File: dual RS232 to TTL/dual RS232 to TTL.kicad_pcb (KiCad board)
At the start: 2 copper layers, 51 x 15.9 mm, 11 parts, among them J1 Conn2x4, J2 Conn2x3, U1 MAX3232EEUE

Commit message: PCB acabada
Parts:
- J1: footprint Connector_Molex:Molex_Nano-Fit_105314-xx08_2x04_P2.50mm_Horizontal -> Herranz - Conn Molex:Molex_Nano-Fit_105314-xx08_2x04_P2.50mm_Horizontal
- J2: footprint Connector_Molex:Molex_Nano-Fit_105314-xx06_2x03_P2.50mm_Horizontal -> Herranz - Conn Molex:Molex_Nano-Fit_105314-xx06_2x03_P2.50mm_Horizontal
- moved C4 4.35 mm to (108.9, 78.8), turned to 90 degrees
- moved C2 4.04 mm to (107.6, 78.8), turned to 90 degrees
- moved C1 3.35 mm to (105.9, 80.3)
- moved F1 2.49 mm to (103.5, 79.3)
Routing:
- net +3V3: track 7.69 -> 5.18 mm
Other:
- board text added: "Dual RS232 to TTL"
- board text added: "https://github.com/herranz/dual-rs232-to-ttl"

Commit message: añadido de la licencia en la PCB
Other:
- board text added: "CERN-OHL-W"

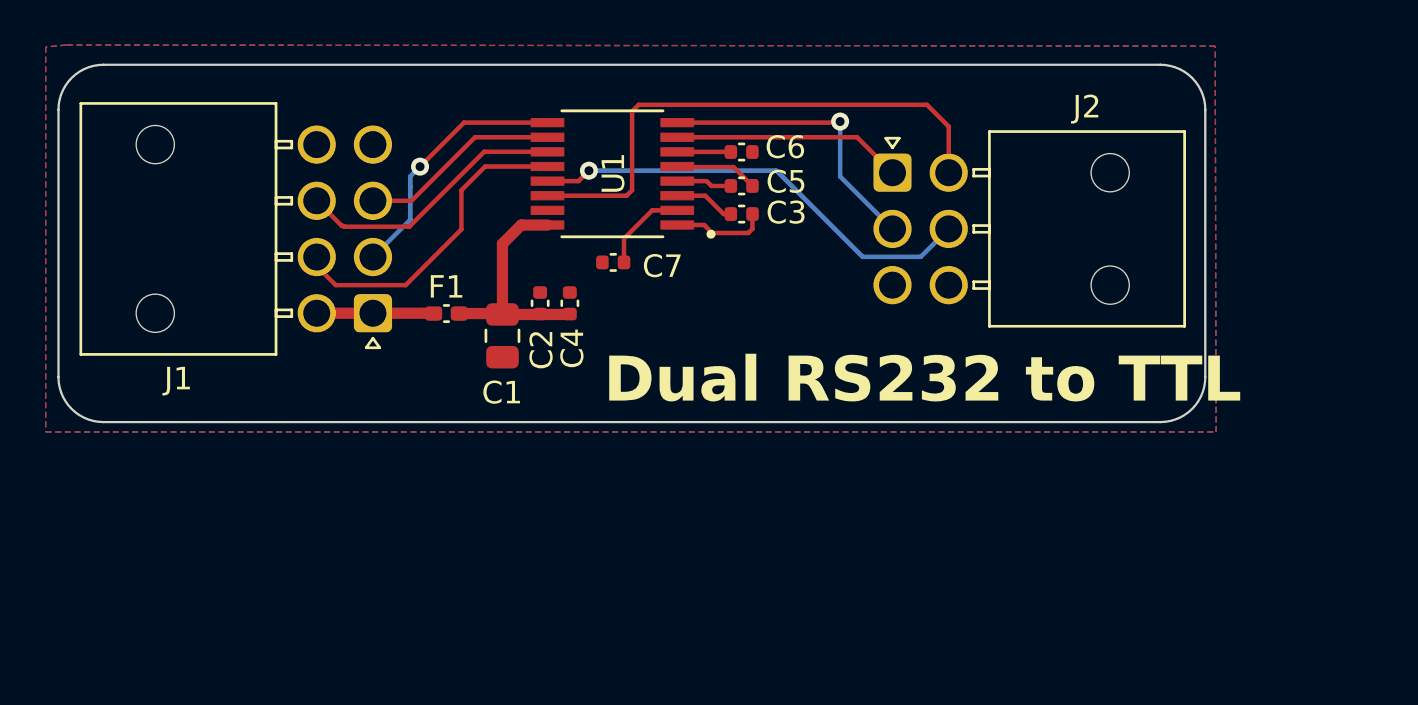
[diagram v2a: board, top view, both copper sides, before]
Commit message: Añadido agujero al PCB y Creado el archivo de producción
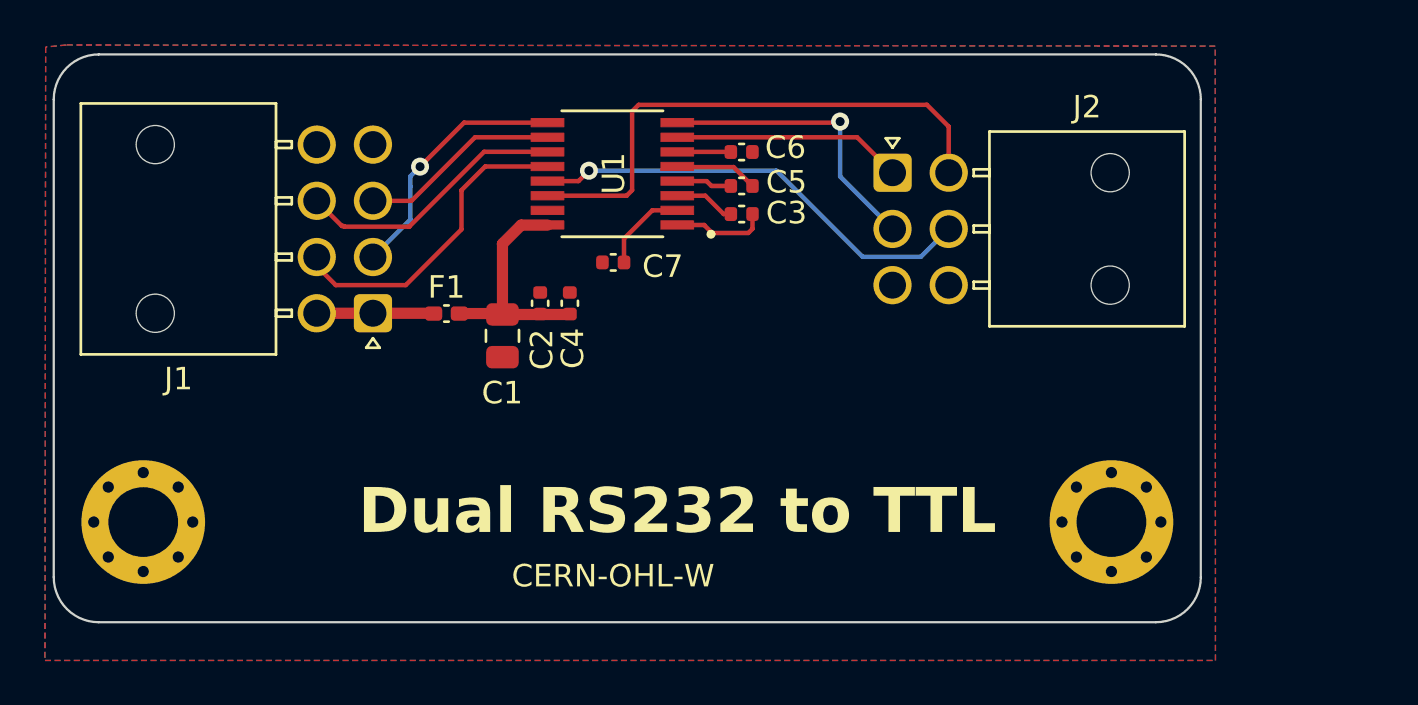
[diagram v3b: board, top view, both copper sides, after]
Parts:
- added MC1: M3_Hole, Herranz - Various:M3_Hole, F.Cu at (90.0, 88.5)
- added MC2: M3_Hole, Herranz - Various:M3_Hole, F.Cu at (133.0, 88.5)
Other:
- board size 51 x 15.9 mm -> 51 x 25.2 mm
- board text removed: "https://github.com/herranz/dual-rs232-to-ttl"
